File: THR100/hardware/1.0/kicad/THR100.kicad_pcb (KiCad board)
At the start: 2 copper layers, 75 x 75 mm, 51 parts, among them J1 CAN, J2 SWITCHES, J3 ANALOG_IN, J4 Screw_Terminal_01x02, J5 Screw_Terminal_01x02, K1 FINDER-32.21-x300, K2 FINDER-32.21-x300, Q1 NTE123A, Q2 NTE123A, SW1 SCR, SW2 MODE, SW3 INSTANCE, U1 MCP2551-I-P, U2 TMR-1-1211, U3 Teensy_3.2, U4 CNY74-2H

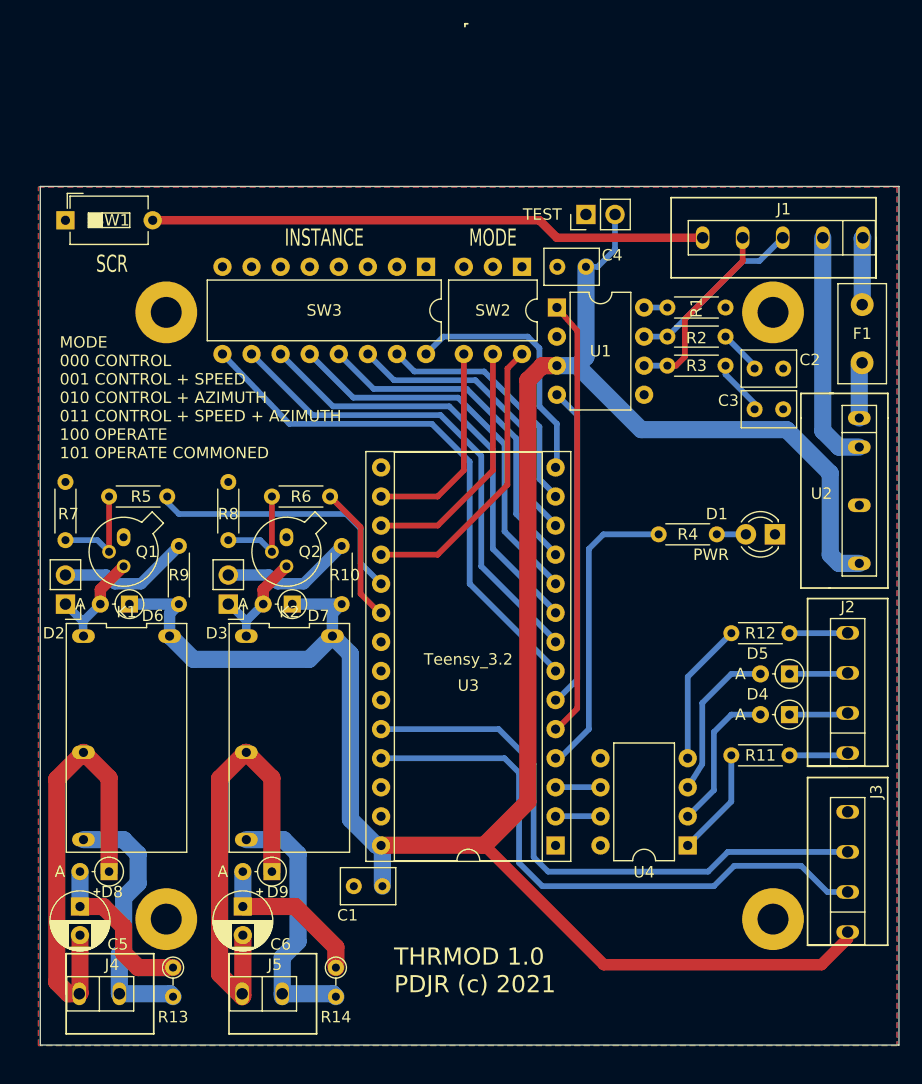
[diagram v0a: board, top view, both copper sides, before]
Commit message: Add switch inputs
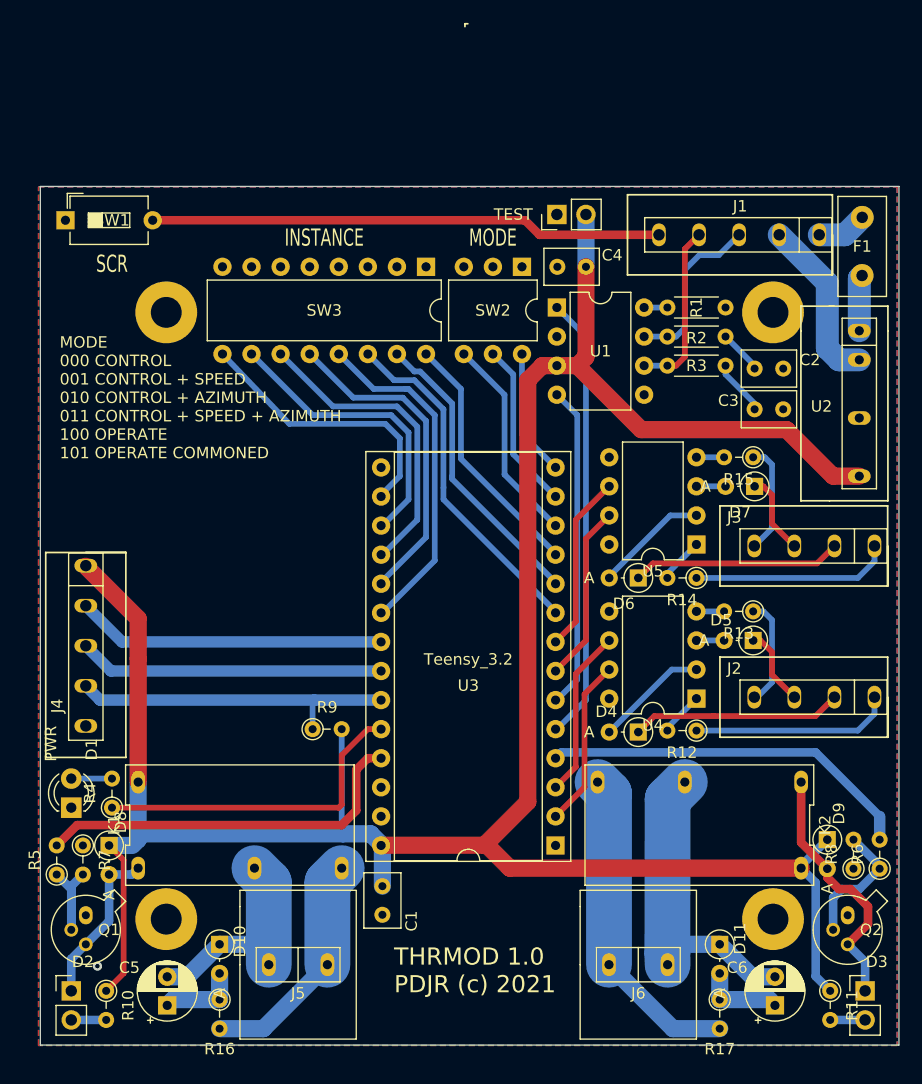
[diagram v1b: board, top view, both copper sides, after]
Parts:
- removed the R12 at (201.6, 126.0)
- added D6: 1N4001, Diode_THT:D_DO-34_SOD68_P2.54mm_Vertical_AnodeUp, F.Cu at (188.4, 121.2)
- added D7: 1N4001, Diode_THT:D_DO-34_SOD68_P2.54mm_Vertical_AnodeUp, F.Cu at (198.6, 113.2)
- added J4: ANALOG, PDJR:Phoenix-FK-MPT-5-3,5, F.Cu at (140.1, 132.3)
- added R13: 1K4, Resistor_THT:R_Axial_DIN0204_L3.6mm_D1.6mm_P2.54mm_Vertical, F.Cu at (198.4, 124.1)
- added R14: 1K4, Resistor_THT:R_Axial_DIN0204_L3.6mm_D1.6mm_P2.54mm_Vertical, F.Cu at (193.5, 121.2)
- added R15: 1K4, Resistor_THT:R_Axial_DIN0204_L3.6mm_D1.6mm_P2.54mm_Vertical, F.Cu at (198.4, 110.6)
- added R9: 2K2, Resistor_THT:R_Axial_DIN0204_L3.6mm_D1.6mm_P2.54mm_Vertical, F.Cu at (159.9, 134.4)
- added U5: CNY74-2H, Package_DIP:DIP-8_W7.62mm, F.Cu at (193.5, 118.2)
- J2: value SWITCHES -> SB0
- J3: value ANALOG_IN -> SB1
- J5: renamed from J4; footprint PDJR:Phoenix-FK-MPT-2-3,5 -> PDJR:WUERTH_2015_5.08_x2
- J6: renamed from J5; footprint PDJR:Phoenix-FK-MPT-2-3,5 -> PDJR:WUERTH_2015_5.08_x2
- R10: renamed from R9; footprint Resistor_THT:R_Axial_DIN0204_L3.6mm_D1.6mm_P5.08mm_Horizontal -> Resistor_THT:R_Axial_DIN0204_L3.6mm_D1.6mm_P2.54mm_Vertical
- R11: renamed from R10; footprint Resistor_THT:R_Axial_DIN0204_L3.6mm_D1.6mm_P5.08mm_Horizontal -> Resistor_THT:R_Axial_DIN0204_L3.6mm_D1.6mm_P2.54mm_Vertical
- R12: renamed from R11; footprint Resistor_THT:R_Axial_DIN0204_L3.6mm_D1.6mm_P5.08mm_Horizontal -> Resistor_THT:R_Axial_DIN0204_L3.6mm_D1.6mm_P2.54mm_Vertical
- R4, R5, R6, R7, R8: footprint Resistor_THT:R_Axial_DIN0204_L3.6mm_D1.6mm_P5.08mm_Horizontal -> Resistor_THT:R_Axial_DIN0204_L3.6mm_D1.6mm_P2.54mm_Vertical
- moved D1 65.9 mm to (138.9, 141.2), turned to 90 degrees
- moved D3 65.1 mm to (208.2, 157.2), turned to 0 degrees
- moved R8 64.2 mm to (207.2, 146.6), turned to 90 degrees
- moved R6 62.3 mm to (209.5, 146.6), turned to 90 degrees
- moved Q2 59.1 mm to (206.7, 150.6)
- moved R11 54.4 mm to (205.2, 157.2), turned to 270 degrees
- moved R4 53.4 mm to (142.4, 141.2), turned to 90 degrees
- moved D9 51.1 mm to (204.9, 144.0), turned to 270 degrees
- moved C6 47.3 mm to (200.3, 158.5), turned to 90 degrees
- moved D11 39.6 mm to (195.5, 153.2), turned to 270 degrees
- moved K2 36.6 mm to (193.7, 142.7), turned to 180 degrees
- moved R10 34.4 mm to (141.9, 157.2), turned to 270 degrees
- moved D2 33.8 mm to (138.9, 157.2), turned to 0 degrees
- moved R17 33.6 mm to (195.5, 158.0)
- moved R5 33.3 mm to (137.6, 147.1), turned to 90 degrees
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- renumbered D8 to D10, D9 to D11, D6 to D8, D7 to D9, R13 to R16, R14 to R17
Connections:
- J3 pad 1: +5V -> Net-(J3-Pad1)
- J3 pad 2: /SPEED -> Net-(D6-Pad1)
- J3 pad 3: /AZIMUTH -> Net-(D7-Pad1)
- J3 pad 4: GND -> Net-(J3-Pad4)
- J6 pad 1: /SB_CO -> /SB-NO
- J6 pad 2: /SB-NO -> /SB_CO
- U3 pad 10: /ADDR_4 -> /ADDR_1
- U3 pad 11: /ADDR_3 -> /ADDR_0
- U3 pad 12: /ADDR_2 -> /MODE_ADDR_2
- U3 pad 13: /ADDR_1 -> /MODE_ADDR_1
- U3 pad 14: /ADDR_0 -> /MODE_ADDR_0
- U3 pad 16: /MODE_ADDR_2 -> /ADDR_7
- U3 pad 17: /MODE_ADDR_1 -> /ADDR_6
- U3 pad 18: /MODE_ADDR_0 -> /ADDR_5
- U3 pad 19: /PS_RLY -> /ADDR_4
- U3 pad 20: /SB_RLY -> /ADDR_3
- U3 pad 21: (no net) -> /SPEED
- U3 pad 22: (no net) -> /AZIMUTH
- U3 pad 23: (no net) -> /TEMPERATURE
- U3 pad 24: /AZIMUTH -> /LED_PWR
- U3 pad 25: /SPEED -> /PS_RLY
- U3 pad 4: /LED_PWR -> /SB_RLY
- U3 pad 7: /ADDR_7 -> /RT_CMD
- U3 pad 8: /ADDR_6 -> /PW_CMD
- U3 pad 9: /ADDR_5 -> /ADDR_2
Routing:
- net +5V: track 199.4 -> 236.4 mm
- net /TEMPERATURE: track 0.00 -> 28.9 mm
- net /AZIMUTH: track 51.4 -> 26.7 mm
- net /SPEED: track 51.7 -> 27.1 mm
- net /ADDR_7: track 47.0 -> 24.4 mm
- net /SB_RLY: track 12.1 -> 33.0 mm
- net /PS_CO: track 39.4 -> 19.7 mm
- net Net-(D6-Pad1): track 0.00 -> 18.3 mm
- net Net-(J3-Pad1): track 0.00 -> 17.5 mm
- net /ADDR_6: track 42.7 -> 25.7 mm
- net /RT_CMD: track 0.00 -> 15.5 mm
- net /PW_CMD: track 0.00 -> 15.5 mm
- net /MODE_ADDR_0: track 25.5 -> 11.5 mm
- net /SB_G: track 5.14 -> 18.6 mm
- net Net-(D3-Pad1): track 9.73 -> 22.6 mm
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
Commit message: PCB tweaks
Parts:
- removed the R13 at (198.4, 124.1)
- removed the R9 at (159.9, 134.4)
- added R12: 1K4, Resistor_THT:R_Axial_DIN0204_L3.6mm_D1.6mm_P2.54mm_Vertical, F.Cu at (198.6, 126.6)
- J4: footprint PDJR:Phoenix-FK-MPT-5-3,5 -> PDJR:Phoenix-FK-MPT-6-3,5
- R1, R2, R3: footprint Resistor_THT:R_Axial_DIN0204_L3.6mm_D1.6mm_P5.08mm_Horizontal -> Resistor_THT:R_Axial_DIN0204_L3.6mm_D1.6mm_P2.54mm_Vertical
- SW2: footprint Package_DIP:DIP-6_W7.62mm -> Package_DIP:DIP-8_W7.62mm
- moved C4 10.6 mm to (181.9, 104.4), turned to 270 degrees
- moved J4 10.1 mm to (150.2, 131.4), turned to 0 degrees
- moved R2 5.99 mm to (196.0, 103.3), turned to 90 degrees
- moved R3 5.46 mm to (196.0, 108.1), turned to 90 degrees
- moved R14 3.96 mm to (201.3, 113.3), turned to 90 degrees
- moved TEST 3.94 mm to (185.2, 89.5), turned to 0 degrees
- moved U1 3.82 mm to (185.0, 96.5)
- moved D5 3.68 mm to (202.1, 126.6), turned to 0 degrees
- moved SW2 2.54 mm to (180.8, 94.0)
- moved R1 1.52 mm to (196.0, 96.0), turned to 270 degrees
- renumbered R11 to R10, R12 to R11, R14 to R13, R15 to R14, R16 to R15, R17 to R16, R10 to R9
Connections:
- net Net-(D6-Pad1) renamed /RT_G
- net Net-(D7-Pad1) renamed /PW_G
- net Net-(J3-Pad1) renamed /RT_P
- net Net-(J3-Pad4) renamed /PW_P
- J4 pad 3: /AZIMUTH -> GND
- J4 pad 4: /TEMPERATURE -> GND
- J4 pad 5: GND -> /AZIMUTH
- SW2 pad 4: /MODE_ADDR_2 -> GND
- SW2 pad 5: /MODE_ADDR_1 -> /MODE_ADDR_3
- SW2 pad 6: /MODE_ADDR_0 -> /MODE_ADDR_2
- U3 pad 10: /ADDR_1 -> /ADDR_0
- U3 pad 11: /ADDR_0 -> /MODE_ADDR_3
- U3 pad 21: /SPEED -> /ADDR_2
- U3 pad 22: /AZIMUTH -> /SPEED
- U3 pad 23: /TEMPERATURE -> /AZIMUTH
- U3 pad 9: /ADDR_2 -> /ADDR_1
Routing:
- net /TEMPERATURE: track 28.9 -> 0.00 mm
- net /MODE_ADDR_3: track 0.00 -> 20.9 mm
- net /AZIMUTH: track 26.7 -> 16.0 mm
- net Net-(D5-Pad2): track 2.41 -> 12.6 mm
- net Net-(R14-Pad2): track 2.41 -> 8.45 mm
- net /PS_P: track 9.59 -> 4.96 mm
- net /PW_P: track 9.67 -> 6.25 mm
- net /CAN_TX: track 39.1 -> 41.9 mm
- net /ADDR_0: track 22.2 -> 25.0 mm
- net /CAN_L: track 15.1 -> 17.6 mm
- net /CAN_SCR: track 44.8 -> 47.2 mm
- net /ADDR_1: track 26.4 -> 28.7 mm
- net Net-(R1-Pad2): track 2.03 -> 4.27 mm
- net /PS_G: track 6.82 -> 4.99 mm
- net /SPEED: track 27.1 -> 25.4 mm
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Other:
- board text added: "+5"
- board text added: "0"
- board text added: "1"
- board text added: "2"
- board text added: "3"
- board text added: "4"
- board text added: "5"
- board text added: "6"
- board text added: "7"
- board text added: "AZ"
- board text added: "GND"
- board text added: "MODE 3 OFF -> SWITCH MODULE MODE 2 -> POWER MODE 1 -> RETRACT MODE 0 -> ANALOG MODE 3 ON -> RELAY MODULE MODE 2 -> COMMON"
- board text added: "PS"
- board text added: "PW"
- board text added: "RT"
- board text added: "SB"
- board text added: "SP"
- board text added: "SW0"
- board text added: "SW1"
- board text removed: "MODE 000 CONTROL 001 CONTROL + SPEED 010 CONTROL + AZIMUTH 011 CONTROL + SPEED + AZIMUTH 100 OPERATE 101 OPERATE COMMONED"
